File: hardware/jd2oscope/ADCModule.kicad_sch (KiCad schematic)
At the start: 16 parts, among them J2 CONBNC001, U4 ADS7279IPW, U7 OPA192IDBVR

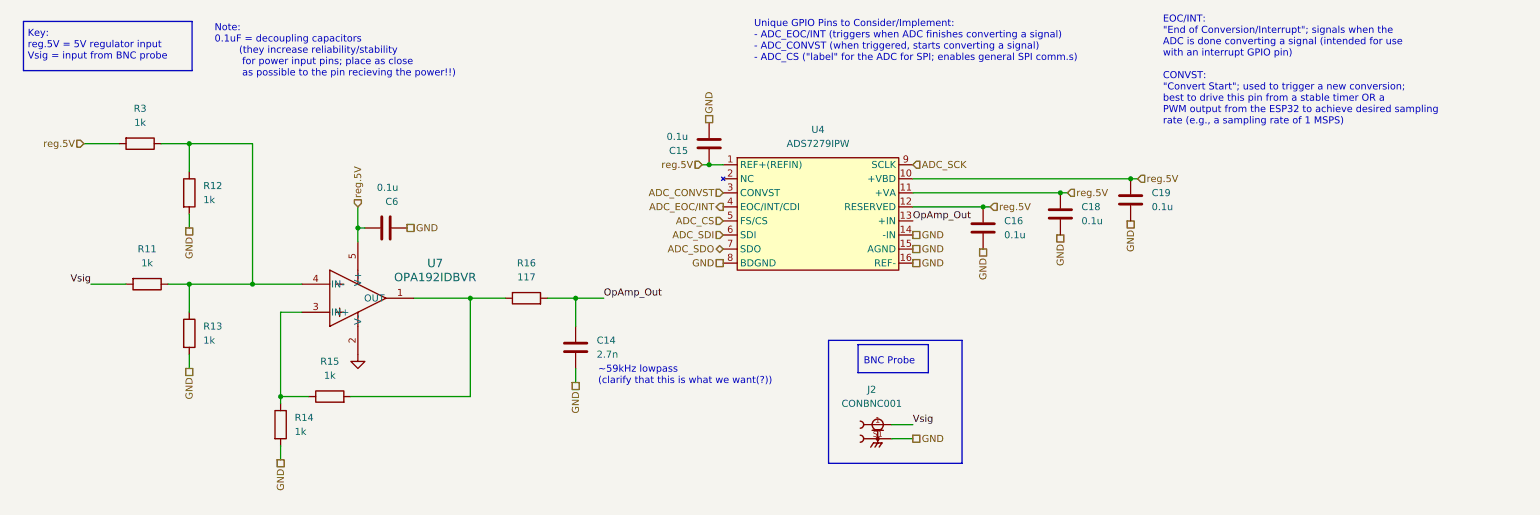
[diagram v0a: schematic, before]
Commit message: feat/fix: no more errors for PCB import too!
Now both the ERC, and the schematic import (and my OCD) are completely satisfied, and we can dev the actual PCB; let's go!! :D
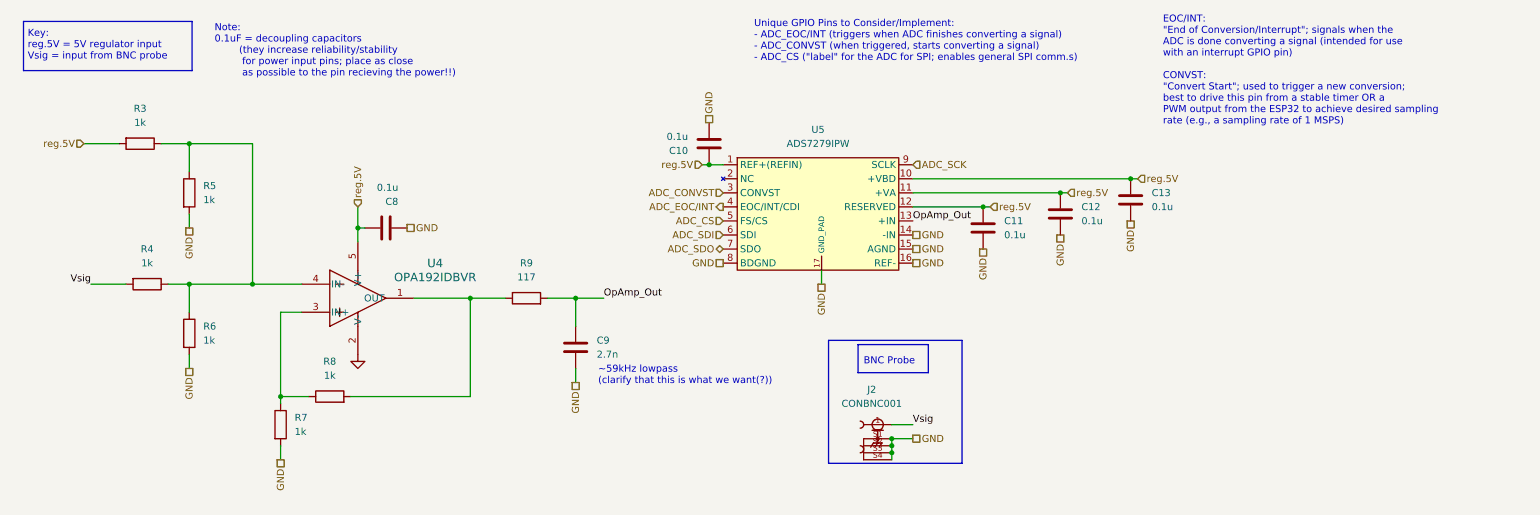
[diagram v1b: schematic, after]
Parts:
- J2: footprint CONBNC001:LINX_CONBNC001 -> jd2Oscope_Footprints:LINX_CONBNC001
- renumbered C15 to C10, C16 to C11, C18 to C12, C19 to C13, C6 to C8, C14 to C9, R11 to R4, R12 to R5, R13 to R6, R14 to R7, R15 to R8, R16 to R9, U7 to U4, U4 to U5
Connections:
- net GND: now also J2.S2, J2.S3, J2.S4, U5.17 (GND_PAD)

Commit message: feat:net lists & net classes implemented
labeled e/a net w/ net labels to clarify nodes, & created net classes w/ desired dimensions for traces; next up is assigning net classes to e/a net & using it to create the pcb!
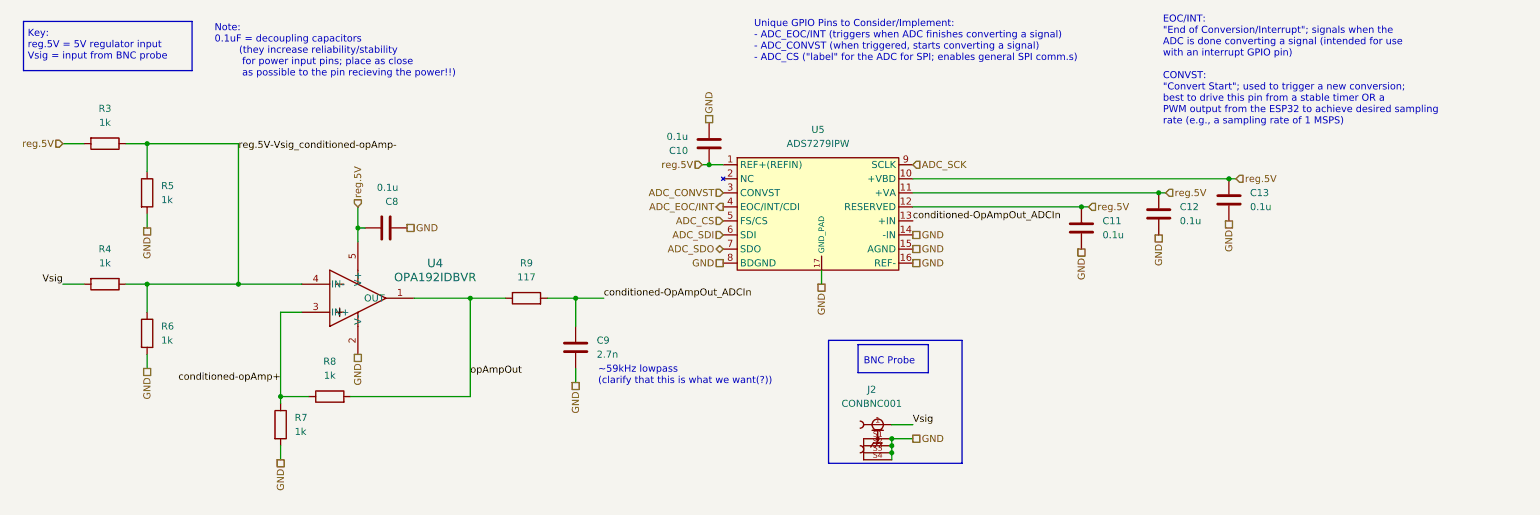
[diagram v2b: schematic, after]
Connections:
- net opAmpOut: now reaches R8.2, R9.1, U4.1 (OUT)
- net conditioned-opAmp+: now reaches R7.1, R8.1, U4.3 (IN+)
- net reg.5V-Vsig_conditioned-opAmp-: now reaches R3.1, R4.1, R5.1, R6.1, U4.4 (IN-)
- net OpAmp_Out renamed conditioned-OpAmpOut_ADCIn
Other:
- moved on the sheet: C11, C12, C13, R3, R4, R5, R6

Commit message: feat: filled in title block
added relevant information to schematic title block blurb in the lower right
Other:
- title: (none) -> 2CH 1MS/s 12b 50kHz 5V Oscope w/320x240 TFT & ESP32
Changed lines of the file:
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@@
 	(generator_version "8.0")
 	(paper "A4")
+	(title_block
+		(title "2CH 1MS/s 12b 50kHz 5V Oscope w/320x240 TFT & ESP32")
+		(date "2025-02-26")
+		(rev "1")
+	)
 	(junction
 		(at 54.61 63.5)

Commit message: fix: propagated group name to all sheets
before it was just on the root; forgot to click the "apply to all sheets" textbox thingie
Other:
- company: (none) -> Group 15
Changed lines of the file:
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@@
 		(date "2025-02-26")
 		(rev "1")
+		(company "Group 15")
 	)
 	(junction

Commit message: fix: schematic labels
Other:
- title: 2CH 1MS/s 12b 50kHz 5V Oscope w/320x240 TFT & ESP32 -> 2CH 1MS/s 14b 50kHz 5V Oscope w/320x240 TFT & ESP32
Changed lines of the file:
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@@
 	(paper "A4")
 	(title_block
-		(title "2CH 1MS/s 12b 50kHz 5V Oscope w/320x240 TFT & ESP32")
+		(title "2CH 1MS/s 14b 50kHz 5V Oscope w/320x240 TFT & ESP32")
 		(date "2025-02-26")
 		(rev "1")

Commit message: fix: undid the thing that I thought was a fix
it is actually 12b still lol
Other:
- title: 2CH 1MS/s 14b 50kHz 5V Oscope w/320x240 TFT & ESP32 -> 2CH 1MS/s 12b 50kHz 5V Oscope w/320x240 TFT & ESP32
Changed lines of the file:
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@@
 	(paper "A4")
 	(title_block
-		(title "2CH 1MS/s 14b 50kHz 5V Oscope w/320x240 TFT & ESP32")
+		(title "2CH 1MS/s 12b 50kHz 5V Oscope w/320x240 TFT & ESP32")
 		(date "2025-02-26")
 		(rev "1")

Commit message: feat: testing files
note: they do not really work atm
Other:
- note added: "Note: fix opamp to have +IN and -IN swapped (with current setup it is inverted)"
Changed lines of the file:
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@@
+		)
+	)
+	(text "Note: fix opamp to have +IN and -IN swapped\n(with current setup it is inverted)"
+		(exclude_from_sim no)
+		(at 95.25 101.092 0)
+		(effects
+			(font
+				(size 1.27 1.27)
+			)
 		)
 	)
